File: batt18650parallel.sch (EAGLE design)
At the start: 6 parts

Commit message: Bobby Schulz design review: address
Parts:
- added H1, H2, H3, H4: (no value), bschulz:MOUNTING_HOLE4_NP
- J1: device SparkFun-Connectors:CONN_022.54MM_SCREWTERM -> bschulz:CONN_022.54_SCREW
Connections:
- net B+: now also S2.NC; no longer S2.COM
- net GND: now also J1.2; no longer J1.1
- net VCC: now also J1.1, S2.COM; no longer J1.2, S2.NC
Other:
- moved on the sheet: J1, J2
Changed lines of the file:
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@@
 <part name="SUPPLY1" library="SparkFun-PowerSymbols" library_urn="urn:adsk.eagle:library:530" deviceset="VCC" device=""/>
 <part name="GND1" library="SparkFun-PowerSymbols" library_urn="urn:adsk.eagle:library:530" deviceset="GND" device=""/>
-<part name="J1" library="SparkFun-Connectors" deviceset="CONN_02" device="2.54MM_SCREWTERM"/>
+<part name="J1" library="bschulz" deviceset="CONN_02" device="2.54_SCREW"/>
 <part name="SUPPLY2" library="SparkFun-PowerSymbols" library_urn="urn:adsk.eagle:library:530" deviceset="VCC" device=""/>
 <part name="GND2" library="SparkFun-PowerSymbols" library_urn="urn:adsk.eagle:library:530" deviceset="GND" device=""/>
@@
 <part name="GND5" library="SparkFun-PowerSymbols" library_urn="urn:adsk.eagle:library:530" deviceset="GND" device=""/>
 <part name="GND6" library="SparkFun-PowerSymbols" library_urn="urn:adsk.eagle:library:530" deviceset="GND" device=""/>
+<part name="H1" library="bschulz" deviceset="MOUNTING_HOLE" device="4_NP"/>
+<part name="H2" library="bschulz" deviceset="MOUNTING_HOLE" device="4_NP"/>
+<part name="H3" library="bschulz" deviceset="MOUNTING_HOLE" device="4_NP"/>
+<part name="H4" library="bschulz" deviceset="MOUNTING_HOLE" device="4_NP"/>
 </parts>
 <sheets>
@@
 <attribute name="NAME" x="71.12" y="72.136" size="2.54" layer="95" align="top-left"/>
 </instance>
-<instance part="SUPPLY1" gate="G$1" x="68.58" y="109.22">
-<attribute name="VALUE" x="68.58" y="112.014" size="1.778" layer="96" align="bottom-center"/>
+<instance part="SUPPLY1" gate="G$1" x="60.96" y="109.22">
+<attribute name="VALUE" x="60.96" y="112.014" size="1.778" layer="96" align="bottom-center"/>
 </instance>
 <instance part="GND1" gate="1" x="50.8" y="50.8">
 <attribute name="VALUE" x="50.8" y="50.546" size="1.778" layer="96" align="top-center"/>
 </instance>
-<instance part="J1" gate="G$1" x="81.28" y="38.1">
-<attribute name="VALUE" x="78.74" y="33.274" size="1.778" layer="96" font="vector"/>
-<attribute name="NAME" x="78.74" y="43.688" size="1.778" layer="95" font="vector"/>
+<instance part="J1" gate="G$1" x="106.68" y="40.64" rot="R180">
+<attribute name="VALUE" x="109.22" y="45.466" size="1.778" layer="96" font="vector" rot="R180"/>
+<attribute name="NAME" x="109.22" y="35.052" size="1.778" layer="95" font="vector" rot="R180"/>
 </instance>
 <instance part="SUPPLY2" gate="G$1" x="96.52" y="48.26">
@@
 <attribute name="VALUE" x="68.58" y="91.186" size="1.778" layer="96" align="top-center"/>
 </instance>
-<instance part="J2" gate="G$1" x="111.76" y="38.1">
-<attribute name="VALUE" x="109.22" y="33.274" size="1.778" layer="96" font="vector"/>
-<attribute name="NAME" x="109.22" y="43.688" size="1.778" layer="95" font="vector"/>
+<instance part="J2" gate="G$1" x="116.84" y="38.1">
+<attribute name="VALUE" x="114.3" y="33.274" size="1.778" layer="96" font="vector"/>
+<attribute name="NAME" x="114.3" y="43.688" size="1.778" layer="95" font="vector"/>
 </instance>
 <instance part="J3" gate="G$1" x="-2.54" y="38.1">
@@
 <attribute name="VALUE" x="104.14" y="91.186" size="1.778" layer="96" align="top-center"/>
 </instance>
+<instance part="H1" gate="G$1" x="40.64" y="27.94">
+<attribute name="NAME" x="42.672" y="28.5242" size="1.778" layer="95"/>
+<attribute name="VALUE" x="42.672" y="25.4762" size="1.778" layer="96"/>
+</instance>
+<instance part="H2" gate="G$1" x="50.8" y="27.94">
+<attribute name="NAME" x="52.832" y="28.5242" size="1.778" layer="95"/>
+<attribute name="VALUE" x="52.832" y="25.4762" size="1.778" layer="96"/>
+</instance>
+<instance part="H3" gate="G$1" x="60.96" y="27.94">
+<attribute name="NAME" x="62.992" y="28.5242" size="1.778" layer="95"/>
+<attribute name="VALUE" x="62.992" y="25.4762" size="1.778" layer="96"/>
+</instance>
+<instance part="H4" gate="G$1" x="71.12" y="27.94">
+<attribute name="NAME" x="73.152" y="28.5242" size="1.778" layer="95"/>
+<attribute name="VALUE" x="73.152" y="25.4762" size="1.778" layer="96"/>
+</instance>
 </instances>
 <busses>
@@
 <net name="VCC" class="0">
 <segment>
-<pinref part="J1" gate="G$1" pin="2"/>
-<wire x1="88.9" y1="40.64" x2="96.52" y2="40.64" width="0.1524" layer="91"/>
 <wire x1="96.52" y1="40.64" x2="96.52" y2="48.26" width="0.1524" layer="91"/>
 <pinref part="SUPPLY2" gate="G$1" pin="VCC"/>
+<pinref part="J1" gate="G$1" pin="1"/>
+<wire x1="96.52" y1="40.64" x2="99.06" y2="40.64" width="0.1524" layer="91"/>
 </segment>
 <segment>
-<pinref part="S2" gate="G$1" pin="NC"/>
-<wire x1="73.66" y1="104.14" x2="68.58" y2="104.14" width="0.1524" layer="91"/>
 <pinref part="SUPPLY1" gate="G$1" pin="VCC"/>
-<wire x1="68.58" y1="104.14" x2="68.58" y2="109.22" width="0.1524" layer="91"/>
+<wire x1="60.96" y1="101.6" x2="60.96" y2="109.22" width="0.1524" layer="91"/>
+<pinref part="S2" gate="G$1" pin="COM"/>
+<wire x1="60.96" y1="101.6" x2="73.66" y2="101.6" width="0.1524" layer="91"/>
 </segment>
 <segment>
@@
 </segment>
 <segment>
-<wire x1="119.38" y1="40.64" x2="127" y2="40.64" width="0.1524" layer="91"/>
+<wire x1="124.46" y1="40.64" x2="127" y2="40.64" width="0.1524" layer="91"/>
 <wire x1="127" y1="40.64" x2="127" y2="48.26" width="0.1524" layer="91"/>
 <pinref part="SUPPLY4" gate="G$1" pin="VCC"/>
@@
 </segment>
 <segment>
-<pinref part="J1" gate="G$1" pin="1"/>
-<wire x1="88.9" y1="38.1" x2="96.52" y2="38.1" width="0.1524" layer="91"/>
 <wire x1="96.52" y1="38.1" x2="96.52" y2="27.94" width="0.1524" layer="91"/>
 <pinref part="GND2" gate="1" pin="GND"/>
+<pinref part="J1" gate="G$1" pin="2"/>
+<wire x1="99.06" y1="38.1" x2="96.52" y2="38.1" width="0.1524" layer="91"/>
 </segment>
 <segment>
@@
 </segment>
 <segment>
-<wire x1="119.38" y1="38.1" x2="127" y2="38.1" width="0.1524" layer="91"/>
+<wire x1="124.46" y1="38.1" x2="127" y2="38.1" width="0.1524" layer="91"/>
 <wire x1="127" y1="38.1" x2="127" y2="27.94" width="0.1524" layer="91"/>
 <pinref part="GND5" gate="1" pin="GND"/>
@@
 <wire x1="33.02" y1="86.36" x2="33.02" y2="76.2" width="0.1524" layer="91"/>
 <label x="33.02" y="83.82" size="1.778" layer="95"/>
-<pinref part="S2" gate="G$1" pin="COM"/>
-<wire x1="73.66" y1="101.6" x2="50.8" y2="101.6" width="0.1524" layer="91"/>
-<wire x1="50.8" y1="101.6" x2="50.8" y2="86.36" width="0.1524" layer="91"/>
 <wire x1="50.8" y1="86.36" x2="66.04" y2="86.36" width="0.1524" layer="91"/>
 <pinref part="BT2" gate="G$0" pin="ANODE"/>
@@
 <label x="60.96" y="86.36" size="1.778" layer="95"/>
 <junction x="50.8" y="86.36"/>
+<pinref part="S2" gate="G$1" pin="NC"/>
+<wire x1="73.66" y1="104.14" x2="68.58" y2="104.14" width="0.1524" layer="91"/>
+<wire x1="68.58" y1="104.14" x2="68.58" y2="116.84" width="0.1524" layer="91"/>
+<wire x1="68.58" y1="116.84" x2="50.8" y2="116.84" width="0.1524" layer="91"/>
+<wire x1="50.8" y1="116.84" x2="50.8" y2="86.36" width="0.1524" layer="91"/>
 </segment>
 </net>

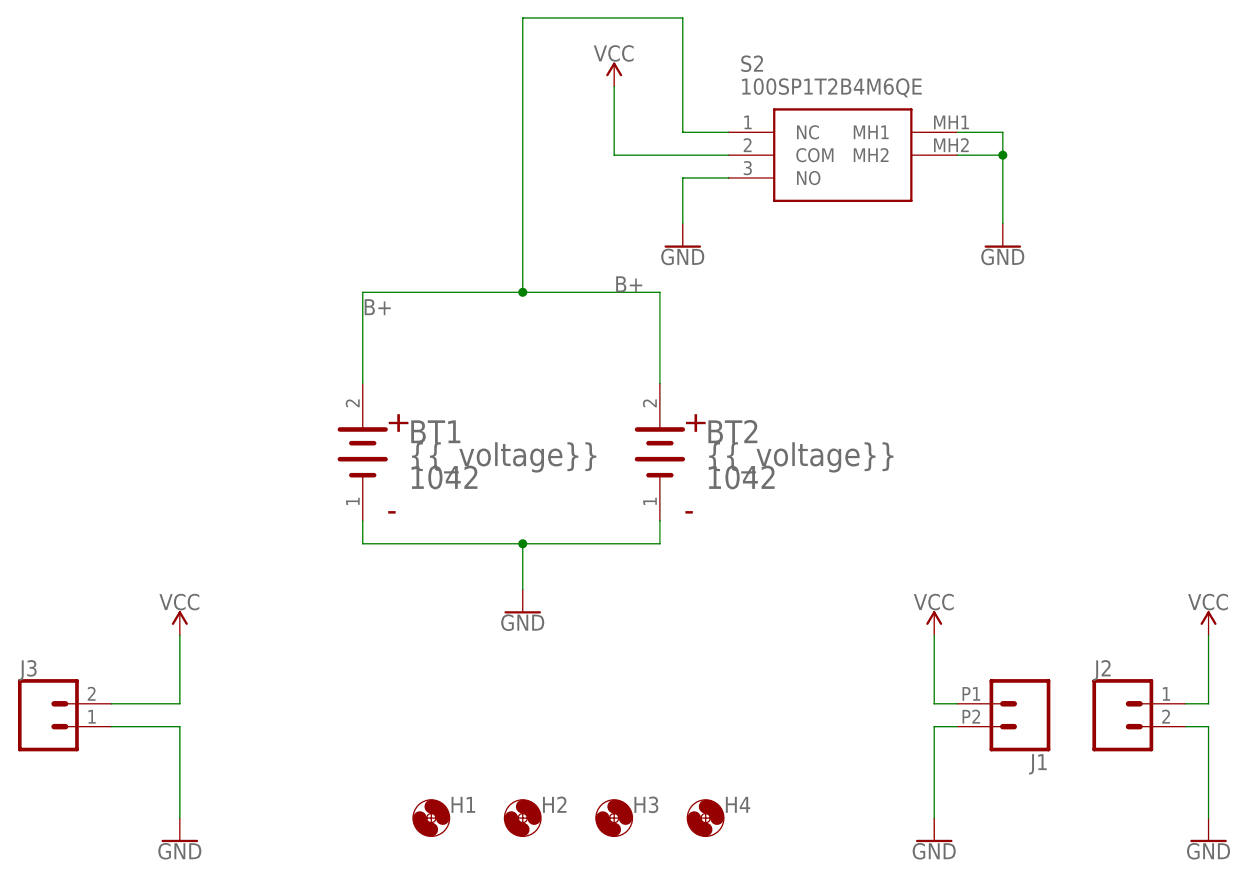
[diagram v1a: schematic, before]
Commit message: Minor updates to connector orientation, pad shape
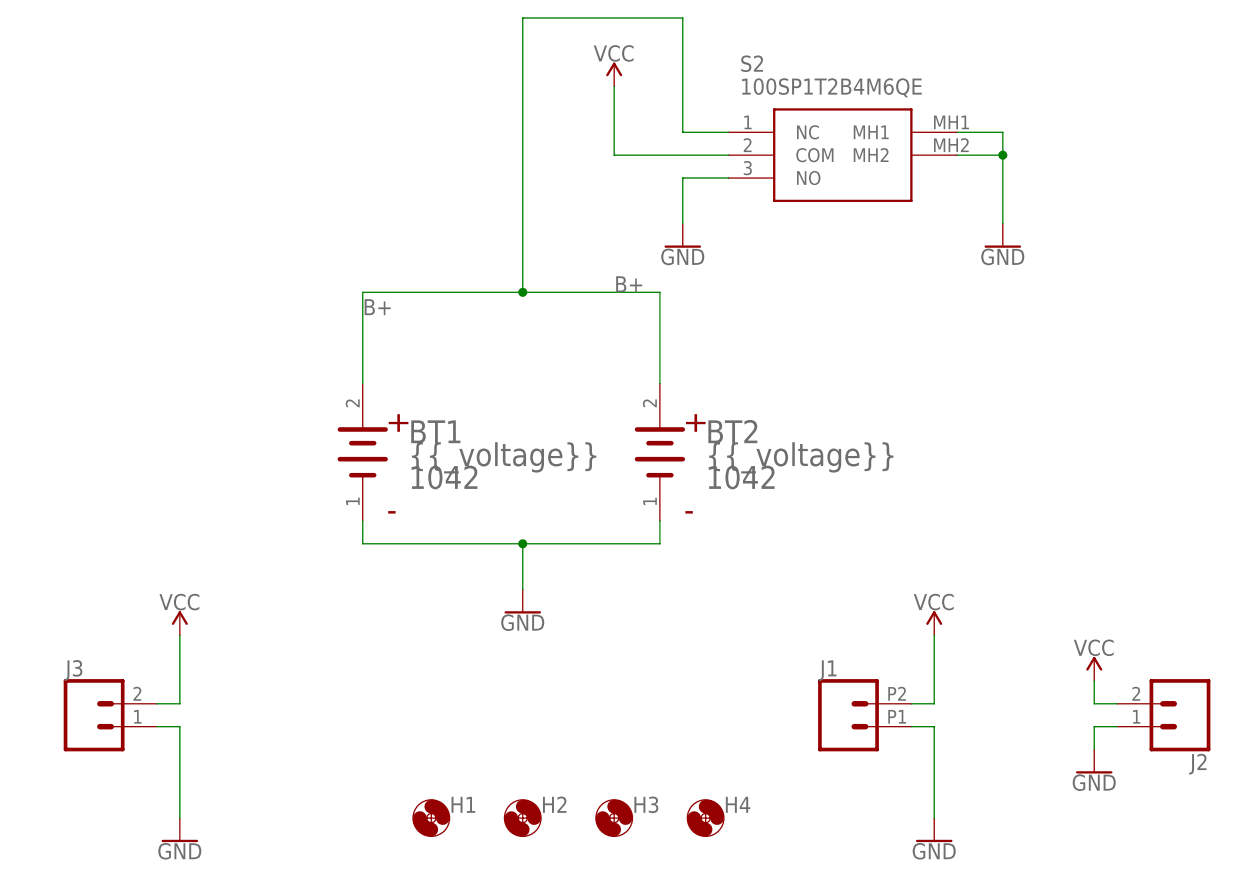
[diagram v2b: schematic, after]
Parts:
- J1: device bschulz:CONN_022.54_SCREW -> bschulz:CONN_022.54_SCREW_ROUND
- J3: device bschulz:CONN_023.5MM_LOCK -> bschulz:CONN_023.5MM_ROUND
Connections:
- net GND: now also J1.1, J2.2; no longer J1.2, J2.1
- net VCC: now also J1.2, J2.1; no longer J1.1, J2.2
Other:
- moved on the sheet: J1, J2, J3
